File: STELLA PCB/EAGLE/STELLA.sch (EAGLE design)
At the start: 51 parts, among them Q1 ECS-.327-5-16-TR, T1 NXP_60_2N7002BKM, T2 NXP_60_2N7002BKM, T3 NXP_60_2N7002BKM, U1 PSSI2021SAY, U10 AD5142BCPZ100, U2 PSSI2021SAY, U4 SN74AUP1G06, U5 SN74AUP1G06, U6 MAX17220ENT+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

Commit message: update
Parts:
- C1, C2: value 4.7uF -> 4.7uF/6.3VDC
- C10, C3, C5, C7, C8, C9: value 0.1uF -> 0.1uF/6.3VDC
- C6, C6A: value 100uF -> 100uF/6.3VDC
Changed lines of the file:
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@@
 <part name="R5" library="UKN_rcl" deviceset="R-EU_" device="R0402" value="10k/1%"/>
 <part name="R6" library="UKN_rcl" deviceset="R-EU_" device="R0402" value="10k/1%"/>
-<part name="C5" library="UKN_rcl" deviceset="C-EU" device="C0402" value="0.1uF"/>
-<part name="C2" library="UKN_rcl" deviceset="C-EU" device="C0402" value="4.7uF"/>
-<part name="C7" library="UKN_rcl" deviceset="C-EU" device="C0402" value="0.1uF"/>
+<part name="C5" library="UKN_rcl" deviceset="C-EU" device="C0402" value="0.1uF/6.3VDC"/>
+<part name="C2" library="UKN_rcl" deviceset="C-EU" device="C0402" value="4.7uF/6.3VDC"/>
+<part name="C7" library="UKN_rcl" deviceset="C-EU" device="C0402" value="0.1uF/6.3VDC"/>
 <part name="X5" library="MyVia" deviceset="5PIN" device=""/>
 <part name="GND15" library="supply1" deviceset="GND" device=""/>
 <part name="GND16" library="supply1" deviceset="GND" device=""/>
 <part name="LED1" library="eZ430-RF2500T_HW-V1.0_20070403" deviceset="LED_LED" device="CHIP-LED0603" value="KPT1608LVSECK-J3-PRV"/>
-<part name="C6A" library="eZ430-RF2500T_HW-V1.0_20070403" deviceset="RCL_C-EU" device="C0805" value="100uF"/>
-<part name="C6" library="eZ430-RF2500T_HW-V1.0_20070403" deviceset="RCL_C-EU" device="C0805" value="100uF"/>
+<part name="C6A" library="eZ430-RF2500T_HW-V1.0_20070403" deviceset="RCL_C-EU" device="C0805" value="100uF/6.3VDC"/>
+<part name="C6" library="eZ430-RF2500T_HW-V1.0_20070403" deviceset="RCL_C-EU" device="C0805" value="100uF/6.3VDC"/>
 <part name="U1" library="PSSI2021SAY" deviceset="PSSI2021SAY" device=""/>
 <part name="P+14" library="supply1" deviceset="VCC" device=""/>
 <part name="GND23" library="supply1" deviceset="GND" device=""/>
 <part name="R3" library="UKN_rcl" deviceset="R-EU_" device="R0402" value="1k/1%"/>
-<part name="C1" library="UKN_rcl" deviceset="C-EU" device="C0402" value="4.7uF"/>
+<part name="C1" library="UKN_rcl" deviceset="C-EU" device="C0402" value="4.7uF/6.3VDC"/>
 <part name="GND27" library="supply1" deviceset="GND" device=""/>
 <part name="P+18" library="supply1" deviceset="VCC" device=""/>
@@
 <part name="GND12" library="supply1" deviceset="GND" device=""/>
 <part name="GND13" library="supply1" deviceset="GND" device=""/>
-<part name="C3" library="UKN_rcl" deviceset="C-EU" device="C0402" value="0.1uF"/>
+<part name="C3" library="UKN_rcl" deviceset="C-EU" device="C0402" value="0.1uF/6.3VDC"/>
 <part name="GND18" library="supply1" deviceset="GND" device=""/>
-<part name="C8" library="UKN_rcl" deviceset="C-EU" device="C0402" value="0.1uF"/>
+<part name="C8" library="UKN_rcl" deviceset="C-EU" device="C0402" value="0.1uF/6.3VDC"/>
 <part name="GND20" library="supply1" deviceset="GND" device=""/>
-<part name="C10" library="UKN_rcl" deviceset="C-EU" device="C0402" value="0.1uF"/>
+<part name="C10" library="UKN_rcl" deviceset="C-EU" device="C0402" value="0.1uF/6.3VDC"/>
 <part name="U$1" library="UKN_schematic-port" deviceset="L_PORT" device=""/>
 <part name="U$2" library="UKN_schematic-port" deviceset="L_PORT" device=""/>
@@
 <part name="T1" library="stella2.1_bilateral_MainPCB" deviceset="NXP_60_2N7002B" device="" technology="KM"/>
 <part name="U$42" library="UKN_schematic-port" deviceset="L_PORT" device=""/>
-<part name="C9" library="UKN_rcl" deviceset="C-EU" device="C0402" value="0.1uF"/>
+<part name="C9" library="UKN_rcl" deviceset="C-EU" device="C0402" value="0.1uF/6.3VDC"/>
 <part name="GND25" library="supply1" deviceset="GND" device=""/>
 <part name="U$43" library="UKN_schematic-port" deviceset="L_PORT" device=""/>
@@
 </instance>
 <instance part="P+4" gate="VCC" x="210.82" y="83.82" smashed="yes">
-<attribute name="VALUE" x="208.28" y="82.55" size="1.778" layer="96" font="vector" rot="R180"/>
+<attribute name="VALUE" x="208.28" y="85.09" size="1.778" layer="96" font="vector" rot="R180"/>
 </instance>
 <instance part="P+5" gate="VCC" x="101.6" y="73.66" smashed="yes">
@@
 </instance>
 <instance part="C2" gate="G$1" x="137.16" y="68.58" smashed="yes" rot="R270">
-<attribute name="VALUE" x="141.478" y="72.898" size="1.778" layer="96" font="vector" rot="R180"/>
-<attribute name="NAME" x="135.636" y="73.66" size="1.778" layer="95" font="vector"/>
+<attribute name="VALUE" x="146.558" y="65.278" size="1.778" layer="96" font="vector" rot="R180"/>
+<attribute name="NAME" x="135.636" y="71.12" size="1.778" layer="95" font="vector"/>
 </instance>
 <instance part="X5" gate="G$1" x="15.24" y="152.4" smashed="yes" rot="MR180"/>
@@
 </instance>
 <instance part="C6A" gate="G$1" x="10.16" y="101.6" smashed="yes">
-<attribute name="NAME" x="14.224" y="100.711" size="1.778" layer="95" font="vector"/>
-<attribute name="VALUE" x="14.224" y="98.171" size="1.778" layer="96" font="vector"/>
+<attribute name="NAME" x="11.684" y="103.251" size="1.778" layer="95" font="vector"/>
+<attribute name="VALUE" x="18.669" y="87.884" size="1.778" layer="96" font="vector" rot="R90"/>
 </instance>
 <instance part="C6" gate="G$1" x="60.96" y="124.46" smashed="yes">
 <attribute name="NAME" x="63.754" y="123.571" size="1.778" layer="95" font="vector"/>
-<attribute name="VALUE" x="63.754" y="121.031" size="1.778" layer="96" font="vector"/>
+<attribute name="VALUE" x="69.469" y="114.554" size="1.778" layer="96" font="vector" rot="R90"/>
 </instance>
 <instance part="U1" gate="G$1" x="114.3" y="157.48" smashed="yes">
@@
 </instance>
 <instance part="P+14" gate="VCC" x="210.82" y="175.26" smashed="yes">
-<attribute name="VALUE" x="207.01" y="173.99" size="1.778" layer="96" font="vector" rot="R180"/>
+<attribute name="VALUE" x="207.01" y="176.53" size="1.778" layer="96" font="vector" rot="R180"/>
 </instance>
 <instance part="GND23" gate="1" x="210.82" y="134.62" smashed="yes">
@@
 </instance>
 <instance part="C1" gate="G$1" x="137.16" y="160.02" smashed="yes" rot="R270">
-<attribute name="VALUE" x="141.478" y="164.338" size="1.778" layer="96" font="vector" rot="R180"/>
-<attribute name="NAME" x="135.636" y="165.1" size="1.778" layer="95" font="vector"/>
+<attribute name="VALUE" x="146.558" y="156.718" size="1.778" layer="96" font="vector" rot="R180"/>
+<attribute name="NAME" x="135.636" y="162.56" size="1.778" layer="95" font="vector"/>
 </instance>
 <instance part="GND27" gate="1" x="147.32" y="73.66" smashed="yes" rot="R270">
@@
 </instance>
 <instance part="C3" gate="G$1" x="139.7" y="139.7" smashed="yes" rot="R270">
-<attribute name="VALUE" x="141.478" y="144.018" size="1.778" layer="96" font="vector" rot="R180"/>
+<attribute name="VALUE" x="144.018" y="144.018" size="1.778" layer="96" font="vector" rot="R180"/>
 <attribute name="NAME" x="136.144" y="138.43" size="1.778" layer="95" font="vector" rot="R180"/>
 </instance>
@@
 <instance part="U$42" gate="G$2" x="91.44" y="88.9" smashed="yes" rot="R180"/>
 <instance part="U4" gate="G$1" x="205.74" y="152.4" smashed="yes">
-<attribute name="VALUE" x="200.66" y="172.72" size="1.778" layer="96"/>
+<attribute name="VALUE" x="215.9" y="160.02" size="1.778" layer="96"/>
 </instance>
 <instance part="U5" gate="G$1" x="205.74" y="60.96" smashed="yes">
-<attribute name="VALUE" x="200.66" y="81.28" size="1.778" layer="96"/>
+<attribute name="VALUE" x="218.44" y="66.04" size="1.778" layer="96"/>
 </instance>
 <instance part="X1" gate="G$1" x="157.48" y="160.02" smashed="yes" rot="R180"/>
@@
 </instance>
 <instance part="C7" gate="G$1" x="116.84" y="157.48" smashed="yes" rot="R90">
-<attribute name="VALUE" x="122.428" y="161.798" size="1.778" layer="96" font="vector" rot="R180"/>
+<attribute name="VALUE" x="132.588" y="161.798" size="1.778" layer="96" font="vector" rot="R180"/>
 <attribute name="NAME" x="114.046" y="154.94" size="1.778" layer="95" font="vector"/>
 </instance>
@@
 </instance>
 <instance part="C8" gate="G$1" x="15.24" y="88.9" smashed="yes">
-<attribute name="VALUE" x="8.382" y="84.582" size="1.778" layer="96" font="vector"/>
+<attribute name="VALUE" x="9.398" y="76.962" size="1.778" layer="96" font="vector" rot="R90"/>
 <attribute name="NAME" x="11.176" y="88.9" size="1.778" layer="95" font="vector"/>
 </instance>
@@
 </instance>
 <instance part="C10" gate="G$1" x="226.06" y="38.1" smashed="yes">
-<attribute name="VALUE" x="226.822" y="33.782" size="1.778" layer="96" font="vector"/>
+<attribute name="VALUE" x="229.362" y="33.782" size="1.778" layer="96" font="vector"/>
 <attribute name="NAME" x="227.076" y="38.1" size="1.778" layer="95" font="vector"/>
 </instance>

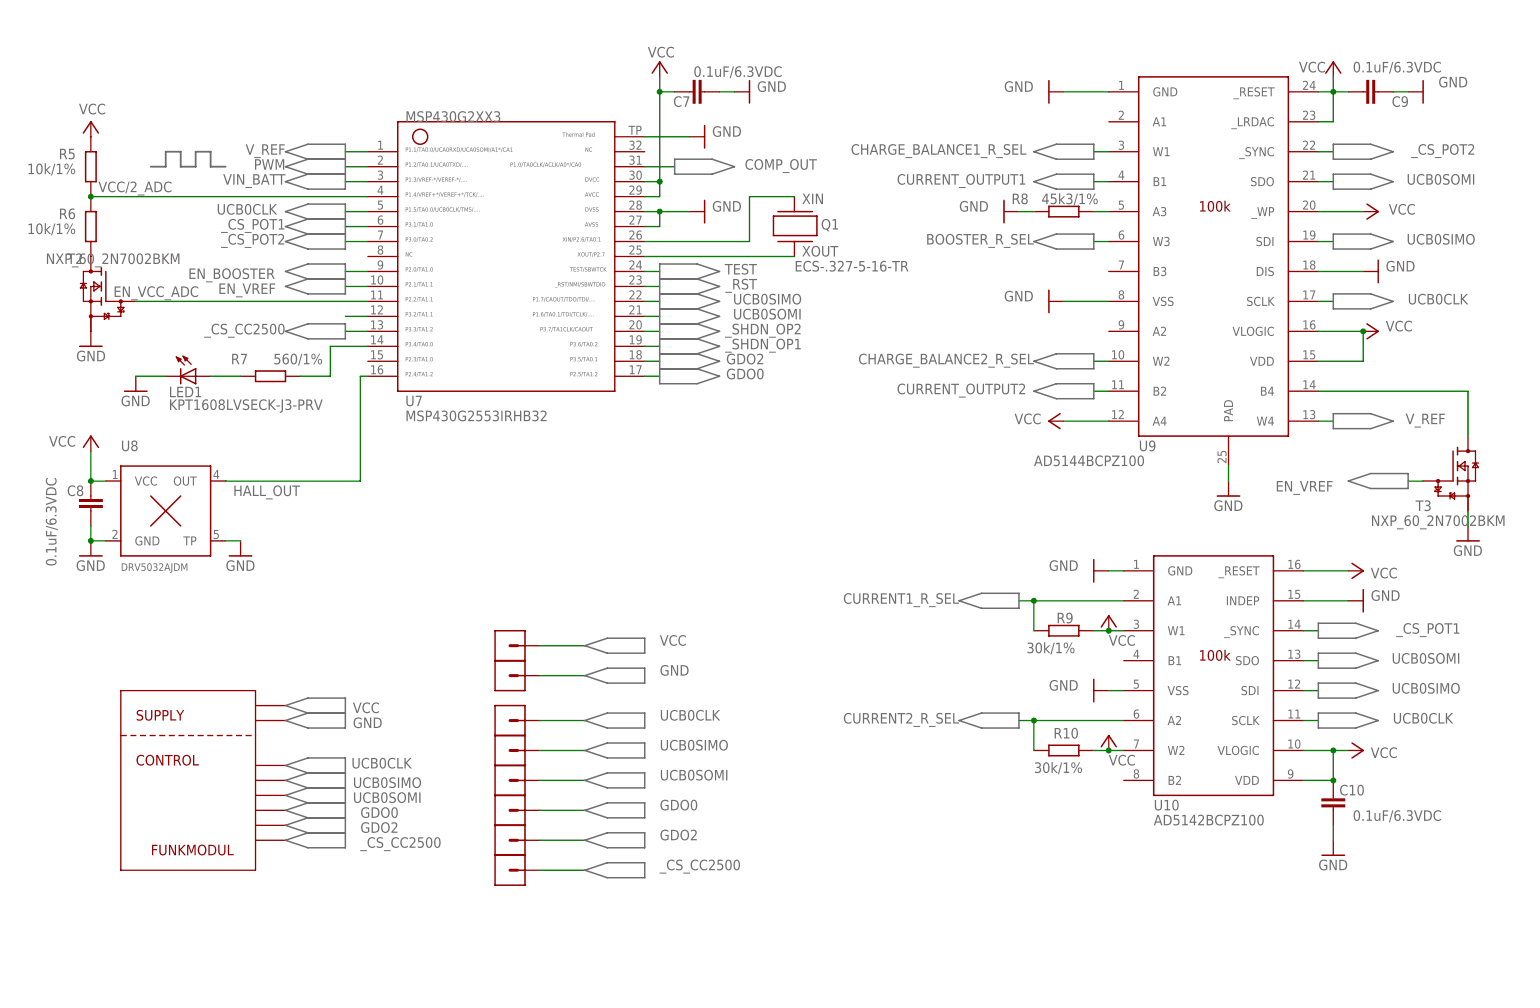
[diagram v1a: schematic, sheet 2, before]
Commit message: - Move BIST measurement point for each channel to the node before the blocking capacitor - Add a 10 MΩ discharge resistor to each output channel - Replace 100 uF capacitors with 22 uF/16VDC versions - Fix several overlap and keepout violations - Improve routing and component placement - Include max voltage ratings in capacitor specs
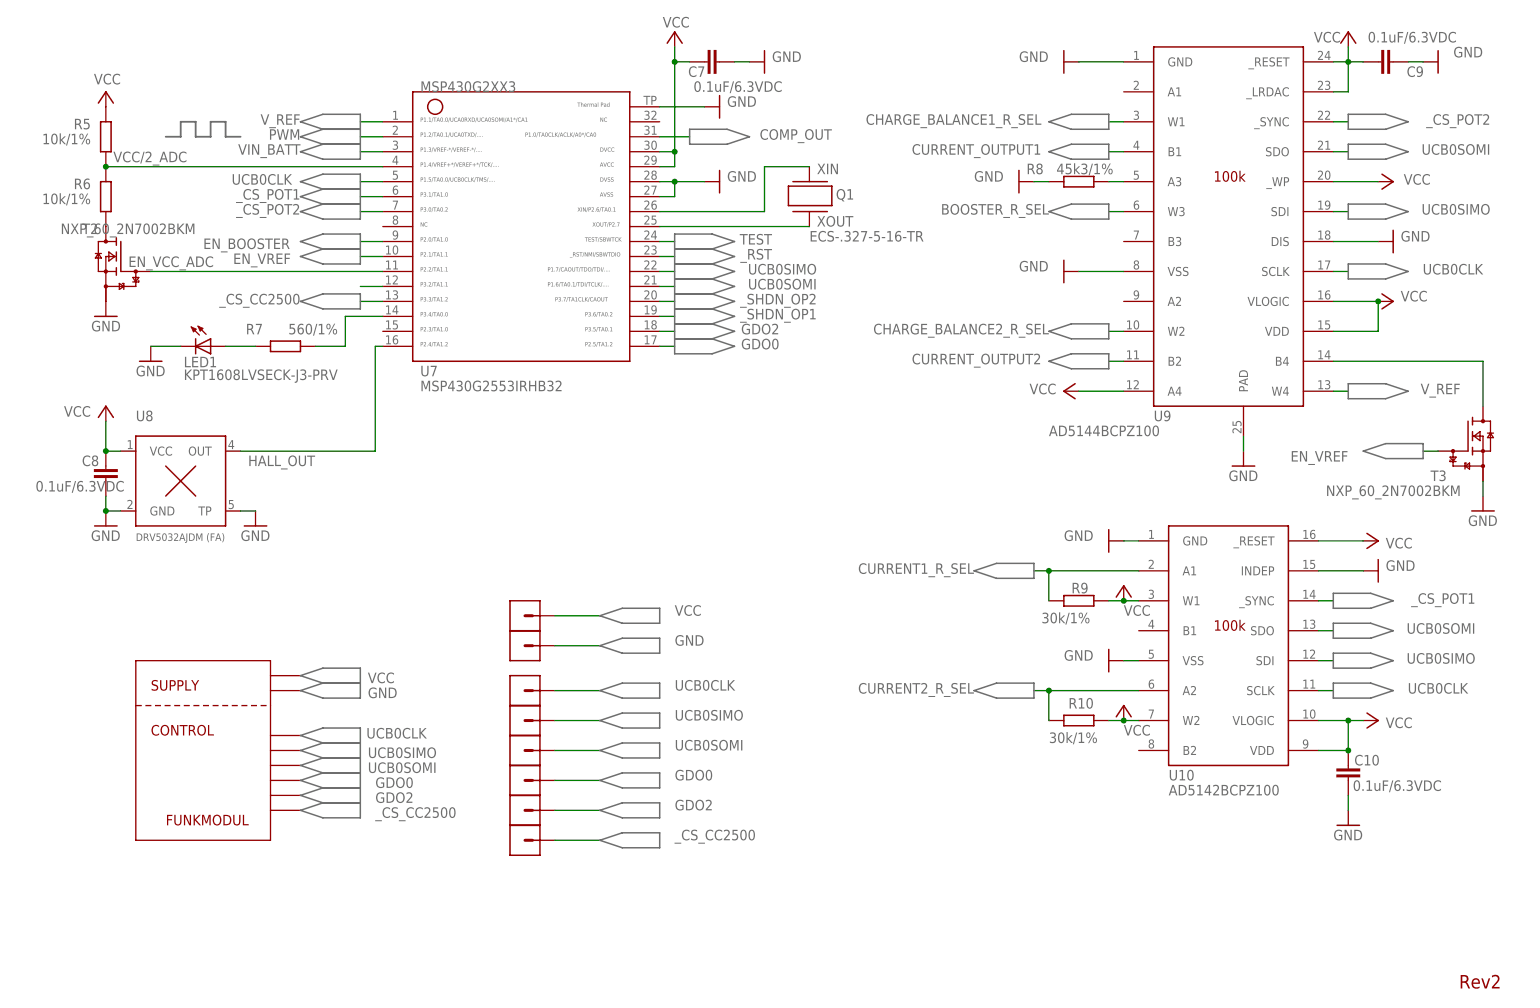
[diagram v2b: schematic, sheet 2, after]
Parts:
- removed C6A: 100uF/6.3VDC, eZ430-RF2500T_HW-V1.0_20070403:RCL_C-EUC0805
- added C4: 22uF/16VDC, UKN_STELLA4_0_1_021022:MYRCL_C0603
- added R11, R12: 10Meg/1%, UKN_rcl:R-EU_R0402
- C6: value 100uF/6.3VDC -> 22uF/16VDC; device eZ430-RF2500T_HW-V1.0_20070403:RCL_C-EUC0805 -> UKN_STELLA4_0_1_021022:MYRCL_C0603
- U8: value DRV5032AJDM -> DRV5032AJDM (FA)
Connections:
- net CURRENT_OUTPUT1: now also U3.IN1+
- net CURRENT_OUTPUT2: now also U3.IN2+
- net GND: now also C4.P$2, C6.P$2, R11.1, R12.2; no longer C6.2, C6A.2
- net STIM_OUT1: now also R11.2; no longer U3.IN1+
- net STIM_OUT2: now also R12.1; no longer U3.IN2+
- net VCC: now also C6.P$1; no longer C6.1
- net VIN_BATT: now also C4.P$1; no longer C6A.1
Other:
- note added: "Rev2"
- note removed: "R0"
- moved on the sheet: C1, C10, C2, C3, C5, C6, C7, C8, C9, L1, LED1, R1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
